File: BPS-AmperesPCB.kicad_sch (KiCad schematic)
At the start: 38 parts, among them J1 Conn_01x04, J2 PeripheralCANConnector, J3 PeripheralCANConnector, U1 PeripheralSOM, U2 INA145UA/2K5, U3 AMC1300BDWV, U4 RO-123.3S_HP

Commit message: layout draft
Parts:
- added C10: 1uF, Capacitor_SMD:C_0805_2012Metric, symbol Device:C
- added C9: 10uF, Capacitor_SMD:C_0805_2012Metric, symbol Device:C
- +12V1: renamed from +12V; footprint (none) -> TestPoint:TestPoint_Keystone_5005-5009_Compact
- +3V3: footprint (none) -> TestPoint:TestPoint_Keystone_5005-5009_Compact
- +3V3High1: renamed from +3V3High; footprint (none) -> TestPoint:TestPoint_Keystone_5005-5009_Compact
- ADC_In1: renamed from ADC_In; footprint (none) -> TestPoint:TestPoint_Keystone_5005-5009_Compact
- C1, C3: value C -> 1uF; footprint (none) -> Capacitor_SMD:C_0805_2012Metric
- C4, C5, C8: footprint (none) -> Capacitor_SMD:C_0805_2012Metric
- C7: value C -> 2.2uF; footprint (none) -> Capacitor_SMD:C_0805_2012Metric
- D2, D3: footprint RBE01VYM6AFHTR -> Parts:RBE01VYM6AFHTR
- GND1: renamed from GND; footprint (none) -> TestPoint:TestPoint_Keystone_5005-5009_Compact
- GNDHigh1: renamed from GNDHigh; footprint (none) -> TestPoint:TestPoint_Keystone_5005-5009_Compact
- GNDPWR1: renamed from GNDPWR; footprint (none) -> TestPoint:TestPoint_Keystone_5005-5009_Compact
- INN1: renamed from INN; footprint (none) -> TestPoint:TestPoint_Keystone_5005-5009_Compact
- INP1: renamed from INP; footprint (none) -> TestPoint:TestPoint_Keystone_5005-5009_Compact
- J1: footprint (none) -> Connector_PinSocket_2.54mm:PinSocket_1x04_P2.54mm_Vertical
- OUTN1: renamed from OUTN; footprint (none) -> TestPoint:TestPoint_Keystone_5005-5009_Compact
- OUTP1: renamed from OUTP; footprint (none) -> TestPoint:TestPoint_Keystone_5005-5009_Compact
- U2: footprint D8 -> Parts:D8
- VOut1: renamed from VOut; footprint (none) -> TestPoint:TestPoint_Keystone_5005-5009_Compact
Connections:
- net +3V3: now also C10.1
- net +3V3 High: now also C9.1
- net GND: now also C10.2
- net GND High: now also C9.2
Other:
- moved on the sheet: +3V3High1, GND1, GNDHigh1

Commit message: tag team
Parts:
- added D4: PowerOn, LED_SMD:LED_0805_2012Metric, symbol Device:LED
- added R9: 1.5k, Resistor_SMD:R_0805_2012Metric, symbol Device:R
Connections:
- net +3V3 High: now also R9.1
- net GND High: now also D4.1 (K)
- new net: D4.2 (A), R9.2
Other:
- moved on the sheet: +3V3, C3, GND1

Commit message: reviewable
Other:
- note added: "303mA"
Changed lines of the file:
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@@
+		)
+	)
+	(text "303mA"
+		(exclude_from_sim no)
+		(at 75.184 46.736 0)
+		(effects
+			(font
+				(size 1.27 1.27)
+			)
 		)
 	)

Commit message: decor fancy
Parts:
- added LOGO1: aniMegamind, Parts:aniMegamind, symbol utsvt-misc:Logo_Placeholder
- added LOGO2: aniMegamind, UTSVT_Special:UTSVT_Logo_Symbol, symbol utsvt-misc:Logo_Placeholder
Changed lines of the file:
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@@
+	)
+	(symbol
+		(lib_id "utsvt-misc:Logo_Placeholder")
+		(at 63.5 74.93 0)
+		(unit 1)
+		(exclude_from_sim no)
+		(in_bom yes)
+		(on_board yes)
+		(dnp no)
+		(fields_autoplaced yes)
+		(property "Reference" "LOGO1"
+			(at 63.5 71.12 0)
+			(effects
+				(font
+					(size 1.27 1.27)
+				)
+				(hide yes)
+			)
+		)
+		(property "Value" "aniMegamind"
+			(at 67.31 74.9299 0)
+			(effects
+				(font
+					(size 1.27 1.27)
+				)
+				(justify left)
+			)
+		)
+		(property "Footprint" "Parts:aniMegamind"
+			(at 63.5 73.025 0)
+			(effects
+				(font
+					(size 1.27 1.27)
+				)
+				(hide yes)
+			)
+		)
+		(property "Datasheet" ""
+			(at 63.5 73.025 0)
+			(effects
+				(font
+					(size 1.27 1.27)
+				)
+				(hide yes)
+			)
+		)
+		(property "Description" "Graph footprint placeholder"
+			(at 63.5 74.93 0)
+			(effects
+				(font
+					(size 1.27 1.27)
+				)
+				(hide yes)
+			)
+		)
+		(instances
+			(project ""
+				(path "/a452d214-ea00-440d-a445-5d6103fda43a"
+					(reference "LOGO1")
+					(unit 1)
+				)
+			)
+		)
 	)
 	(symbol
@@
 					(unit 1)
 				)
+			)
+		)
+	)
+	(symbol
+		(lib_id "utsvt-misc:Logo_Placeholder")
+		(at 63.5 83.82 0)
+		(unit 1)
+		(exclude_from_sim no)
+		(in_bom yes)
+		(on_board yes)
+		(dnp no)
+		(fields_autoplaced yes)
+		(property "Reference" "LOGO2"
+			(at 63.5 80.01 0)
+			(effects
+				(font
+					(size 1.27 1.27)
+				)
+				(hide yes)
+			)
+		)
+		(property "Value" "aniMegamind"
+			(at 67.31 83.8199 0)
+			(effects
+				(font
+					(size 1.27 1.27)
+				)
+				(justify left)
+			)
+		)
+		(property "Footprint" "UTSVT_Special:UTSVT_Logo_Symbol"
+			(at 63.5 81.915 0)
+			(effects
+				(font
+					(size 1.27 1.27)
+				)
+				(hide yes)
+			)
+		)
+		(property "Datasheet" ""
+			(at 63.5 81.915 0)
+			(effects
+				(font
+					(size 1.27 1.27)
+				)
+				(hide yes)
+			)
+		)
+		(property "Description" "Graph footprint placeholder"
+			(at 63.5 83.82 0)
+			(effects
+				(font
+					(size 1.27 1.27)
+				)
+				(hide yes)
+			)
+		)
+		(instances
+			(project "BPS-AmperesPCB"
+				(path "/a452d214-ea00-440d-a445-5d6103fda43a"
+					(reference "LOGO2")
+					(unit 1)
+				)

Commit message: tada
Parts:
- LOGO2: value aniMegamind -> solarlogo
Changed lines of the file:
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@@
 			)
 		)
-		(property "Value" "aniMegamind"
+		(property "Value" "solarlogo"
 			(at 67.31 83.8199 0)
 			(effects

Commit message: bored so i did lhr
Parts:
- renumbered +3V3High1 to +3V3H1, GNDHigh1 to GNDH1, ADC_In1 to aOut1
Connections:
- net ADC_In renamed aOut
- no-connect marks 1 -> 10

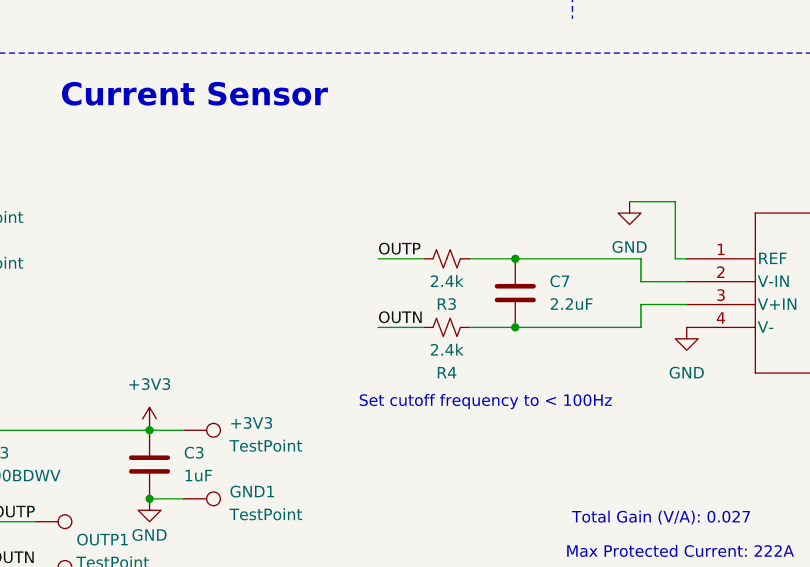
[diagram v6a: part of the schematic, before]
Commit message: fixed outp and outn flip smh
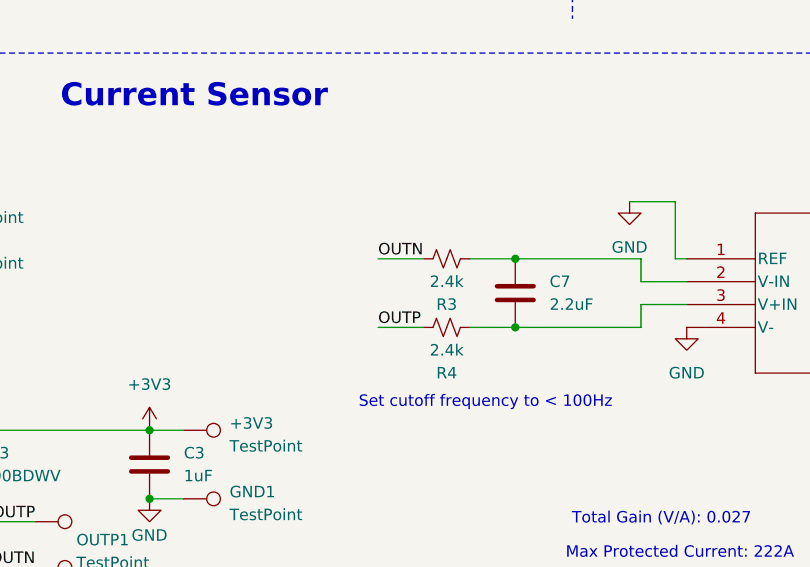
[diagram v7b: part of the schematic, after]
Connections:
- net OUTN: now also R3.2; no longer R4.2
- net OUTP: now also R4.2; no longer R3.2
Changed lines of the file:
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@@
+		)
+	)
+	(label "OUTN"
+		(at 151.13 129.54 0)
+		(effects
+			(font
+				(size 1.27 1.27)
+			)
+			(justify left bottom)
 		)
 	)
@@
 			)
 			(justify right bottom)
+		)
+	)
+	(label "OUTP"
+		(at 151.13 137.16 0)
+		(effects
+			(font
+				(size 1.27 1.27)
+			)
+			(justify left bottom)
 		)
 	)
@@
 		)
 	)
-	(label "OUTN"
-		(at 151.13 137.16 0)
-		(effects
-			(font
-				(size 1.27 1.27)
-			)
-			(justify left bottom)
-		)
-	)
-	(label "OUTP"
-		(at 151.13 129.54 0)
-		(effects
-			(font
-				(size 1.27 1.27)
-			)
-			(justify left bottom)
-		)
-	)
